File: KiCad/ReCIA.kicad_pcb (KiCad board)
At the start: 2 copper layers, 17.4 x 51.4 mm, 1 part, among them U1 8520_DIP

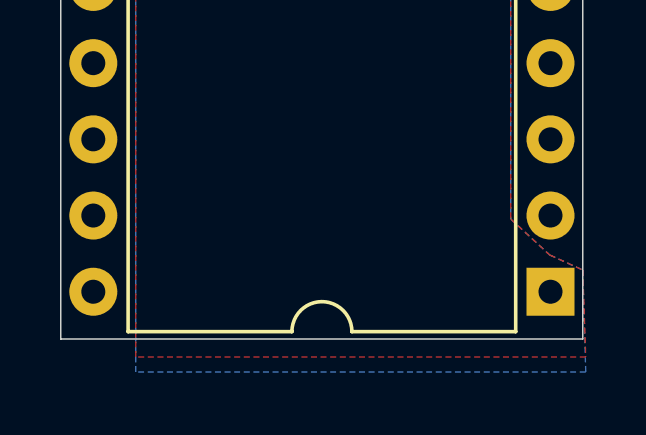
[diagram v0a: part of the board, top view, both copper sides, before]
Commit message: Changed to four layers and fixed clearance and default settings for traces and vias etc
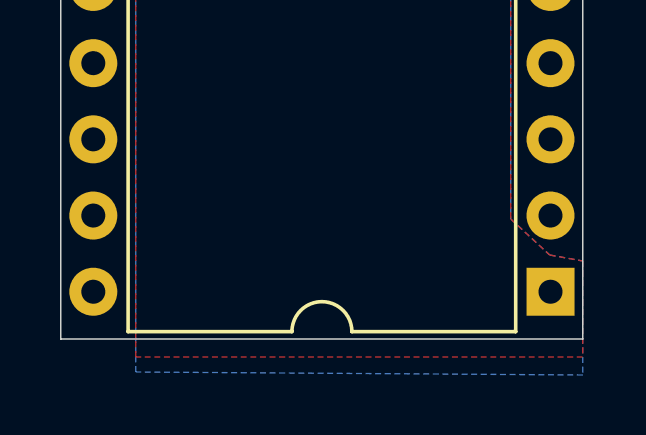
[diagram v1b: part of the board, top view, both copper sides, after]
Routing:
- added copper zone on 3V3, net (none)
- added copper zone on GND, net GND
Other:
- copper layers 2 -> 4
- net class Default: clearance 0.2 -> 0.15; trace_width 0.25 -> 0.15
- rule trace_clearance: 0.2 -> 0.15
- rule trace_min: 0.2 -> 0.15
- rule via_min_drill: 0.3 -> 0.25
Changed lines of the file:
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@@
   (layers
     (0 F.Cu signal)
+    (1 GND power)
+    (2 3V3 power)
     (31 B.Cu signal)
     (32 B.Adhes user)
@@
   )
   (setup
-    (last_trace_width 0.25)
-    (trace_clearance 0.2)
-    (zone_clearance 0.508)
+    (last_trace_width 0.15)
+    (user_trace_width 0.2)
+    (user_trace_width 0.25)
+    (trace_clearance 0.15)
+    (zone_clearance 0.15)
     (zone_45_only no)
-    (trace_min 0.2)
+    (trace_min 0.15)
     (via_size 0.8)
     (via_drill 0.4)
     (via_min_size 0.4)
-    (via_min_drill 0.3)
+    (via_min_drill 0.25)
+    (user_via 0.4 0.25)
     (uvia_size 0.3)
     (uvia_drill 0.1)
@@
   (net 40 GND)
   (net_class Default "This is the default net class."
-    (clearance 0.2)
-    (trace_width 0.25)
+    (clearance 0.15)
+    (trace_width 0.15)
     (via_dia 0.8)
     (via_drill 0.4)
@@
       (effects (font (size 1 1) (thickness 0.15)))
     )
+    (fp_line (start -6.37008 -25.39492) (end 7.35992 -25.39492) (layer F.Fab) (width 0.1))
+    (fp_line (start 7.35992 -25.39492) (end 7.35992 25.40508) (layer F.Fab) (width 0.1))
+    (fp_line (start 7.35992 25.40508) (end -7.37008 25.40508) (layer F.Fab) (width 0.1))
+    (fp_line (start -7.37008 25.40508) (end -7.37008 -24.39492) (layer F.Fab) (width 0.1))
+    (fp_line (start -7.37008 -24.39492) (end -6.37008 -25.39492) (layer F.Fab) (width 0.1))
+    (fp_line (start -1.00508 -25.45492) (end -6.46508 -25.45492) (layer F.SilkS) (width 0.12))
+    (fp_line (start -6.46508 -25.45492) (end -6.46508 25.46508) (layer F.SilkS) (width 0.12))
+    (fp_line (start -6.46508 25.46508) (end 6.45492 25.46508) (layer F.SilkS) (width 0.12))
+    (fp_line (start 6.45492 25.46508) (end 6.45492 -25.45492) (layer F.SilkS) (width 0.12))
+    (fp_line (start 6.45492 -25.45492) (end 0.99492 -25.45492) (layer F.SilkS) (width 0.12))
+    (fp_line (start -8.67508 -25.67492) (end -8.67508 25.67508) (layer F.CrtYd) (width 0.05))
+    (fp_line (start -8.67508 25.67508) (end 8.67492 25.67508) (layer F.CrtYd) (width 0.05))
+    (fp_line (start 8.67492 25.67508) (end 8.67492 -25.67492) (layer F.CrtYd) (width 0.05))
     (fp_line (start 8.67492 -25.67492) (end -8.67508 -25.67492) (layer F.CrtYd) (width 0.05))
-    (fp_line (start 8.67492 25.67508) (end 8.67492 -25.67492) (layer F.CrtYd) (width 0.05))
-    (fp_line (start -8.67508 25.67508) (end 8.67492 25.67508) (layer F.CrtYd) (width 0.05))
-    (fp_line (start -8.67508 -25.67492) (end -8.67508 25.67508) (layer F.CrtYd) (width 0.05))
-    (fp_line (start 6.45492 -25.45492) (end 0.99492 -25.45492) (layer F.SilkS) (width 0.12))
-    (fp_line (start 6.45492 25.46508) (end 6.45492 -25.45492) (layer F.SilkS) (width 0.12))
-    (fp_line (start -6.46508 25.46508) (end 6.45492 25.46508) (layer F.SilkS) (width 0.12))
-    (fp_line (start -6.46508 -25.45492) (end -6.46508 25.46508) (layer F.SilkS) (width 0.12))
-    (fp_line (start -1.00508 -25.45492) (end -6.46508 -25.45492) (layer F.SilkS) (width 0.12))
-    (fp_line (start -7.37008 -24.39492) (end -6.37008 -25.39492) (layer F.Fab) (width 0.1))
-    (fp_line (start -7.37008 25.40508) (end -7.37008 -24.39492) (layer F.Fab) (width 0.1))
-    (fp_line (start 7.35992 25.40508) (end -7.37008 25.40508) (layer F.Fab) (width 0.1))
-    (fp_line (start 7.35992 -25.39492) (end 7.35992 25.40508) (layer F.Fab) (width 0.1))
-    (fp_line (start -6.37008 -25.39492) (end 7.35992 -25.39492) (layer F.Fab) (width 0.1))
     (fp_text user %R (at -0.00508 0.00508) (layer F.Fab) hide
       (effects (font (size 1 1) (thickness 0.15)))
@@
       (net 36 "Net-(U1-Pad22)"))
     (pad 2 thru_hole oval (at -7.62508 -21.58492 180) (size 1.6 1.6) (drill 0.8) (layers *.Cu *.Mask)
-      (net 37 "Net-(U1-Pad2)"))
+      (net 37 "Net-(U1-Pad2)") (clearance 0.5))
     (pad 21 thru_hole oval (at 7.61492 24.13508 180) (size 1.6 1.6) (drill 0.8) (layers *.Cu *.Mask)
       (net 38 "Net-(U1-Pad21)"))
     (pad 1 thru_hole rect (at -7.62508 -24.12492 180) (size 1.6 1.6) (drill 0.8) (layers *.Cu *.Mask)
-      (net 40 GND) (zone_connect 2))
+      (net 40 GND) (zone_connect 2) (thermal_gap 0.5))
   )
   (gr_line (start 123.3 108.7) (end 123.3 57.3) (layer Edge.Cuts) (width 0.05))
@@
   (gr_line (start 123.3 57.3) (end 140.7 57.3) (layer Edge.Cuts) (width 0.05))
   (zone (net 40) (net_name GND) (layer F.Cu) (hatch edge 0.508)
-    (connect_pads (clearance 0.508))
-    (min_thickness 0.254)
-    (fill yes (arc_segments 32) (thermal_gap 0.508) (thermal_bridge_width 0.508))
+    (connect_pads (clearance 0.15))
+    (min_thickness 0.15)
+    (fill yes (arc_segments 32) (thermal_gap 0.15) (thermal_bridge_width 0.3))
     (polygon
       (pts
-        (xy 138.3 104.7) (xy 139.6 105.9) (xy 140.7 106.4) (xy 140.8 109.3) (xy 125.8 109.3)
+        (xy 138.3 104.7) (xy 139.6 105.9) (xy 140.7 106.1) (xy 140.7 109.3) (xy 125.8 109.3)
         (xy 125.8 56.8) (xy 138.3 56.8)
       )
@@
   )
   (zone (net 40) (net_name GND) (layer B.Cu) (hatch edge 0.508)
-    (connect_pads (clearance 0.508))
-    (min_thickness 0.254)
-    (fill yes (arc_segments 32) (thermal_gap 0.508) (thermal_bridge_width 0.508))
+    (connect_pads (clearance 0.15))
+    (min_thickness 0.15)
+    (fill yes (arc_segments 32) (thermal_gap 0.15) (thermal_bridge_width 0.3))
     (polygon
       (pts
-        (xy 138.3 104.7) (xy 139.6 105.9) (xy 140.7 106.4) (xy 140.8 109.8) (xy 125.8 109.8)
+        (xy 138.3 104.7) (xy 139.6 105.9) (xy 140.7 106.1) (xy 140.7 109.9) (xy 125.8 109.8)
         (xy 125.8 56.3) (xy 138.3 56.3)
       )
     )
+  )
+  (zone (net 40) (net_name GND) (layer GND) (hatch edge 0.508)
+    (connect_pads (clearance 0.15))
+    (min_thickness 0.15)
+    (fill yes (arc_segments 32) (thermal_gap 0.15) (thermal_bridge_width 0.3))
+    (polygon
+      (pts
+        (xy 138.3 104.7) (xy 139.6 105.9) (xy 140.7 106.1) (xy 140.7 110.4) (xy 125.8 110.3)
+        (xy 125.8 55.8) (xy 138.3 55.8)
+      )
+    )
+  )
+  (zone (net 0) (net_name "") (layer 3V3) (hatch edge 0.508)
+    (connect_pads (clearance 0.15))
+    (min_thickness 0.15)
+    (fill yes (arc_segments 32) (thermal_gap 0.15) (thermal_bridge_width 0.3))
+    (polygon
+      (pts
+        (xy 138.3 110.9) (xy 125.8 110.9) (xy 125.8 55.3) (xy 138.3 55.3)
+      )
+    )

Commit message: Add nets
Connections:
- net Net-(U1-Pad10) renamed PB0
- net Net-(U1-Pad11) renamed PB1
- net Net-(U1-Pad12) renamed PB2
- net Net-(U1-Pad13) renamed PB3
- net Net-(U1-Pad14) renamed PB4
- net Net-(U1-Pad15) renamed PB5
- net Net-(U1-Pad16) renamed PB6
- net Net-(U1-Pad17) renamed PB7
- net Net-(U1-Pad18) renamed PC
- net Net-(U1-Pad19) renamed TOD
- net Net-(U1-Pad2) renamed PA0
- net Net-(U1-Pad21) renamed IRQ
- net Net-(U1-Pad22) renamed RW
- net Net-(U1-Pad23) renamed CS
- net Net-(U1-Pad24) renamed FLAG
- net Net-(U1-Pad25) renamed E-CLK
- net Net-(U1-Pad26) renamed D7
- net Net-(U1-Pad27) renamed D6
- net Net-(U1-Pad28) renamed D5
- net Net-(U1-Pad29) renamed D4
- net Net-(U1-Pad3) renamed PA1
- net Net-(U1-Pad30) renamed D3
- net Net-(U1-Pad31) renamed D2
- net Net-(U1-Pad32) renamed D1
- net Net-(U1-Pad33) renamed D0
- net Net-(U1-Pad34) renamed RESET
- net Net-(U1-Pad35) renamed A3
- net Net-(U1-Pad36) renamed A2
- net Net-(U1-Pad37) renamed A1
- net Net-(U1-Pad38) renamed A0
- net Net-(U1-Pad39) renamed SP
- net Net-(U1-Pad4) renamed PA2
- net Net-(U1-Pad40) renamed CNT
- net Net-(U1-Pad5) renamed PA3
- net Net-(U1-Pad6) renamed PA4
- net Net-(U1-Pad7) renamed PA5
- net Net-(U1-Pad8) renamed PA6
- net Net-(U1-Pad9) renamed PA7

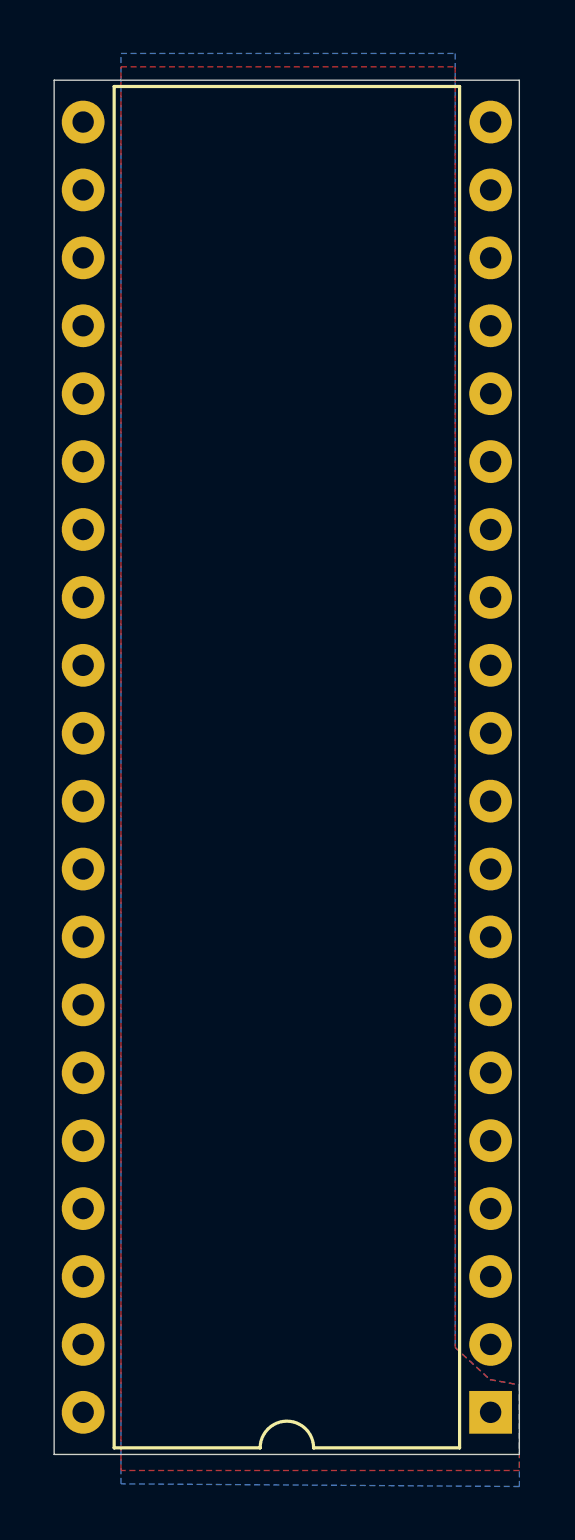
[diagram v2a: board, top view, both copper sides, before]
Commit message: Added a 3.3V LDO Voltage Regulator
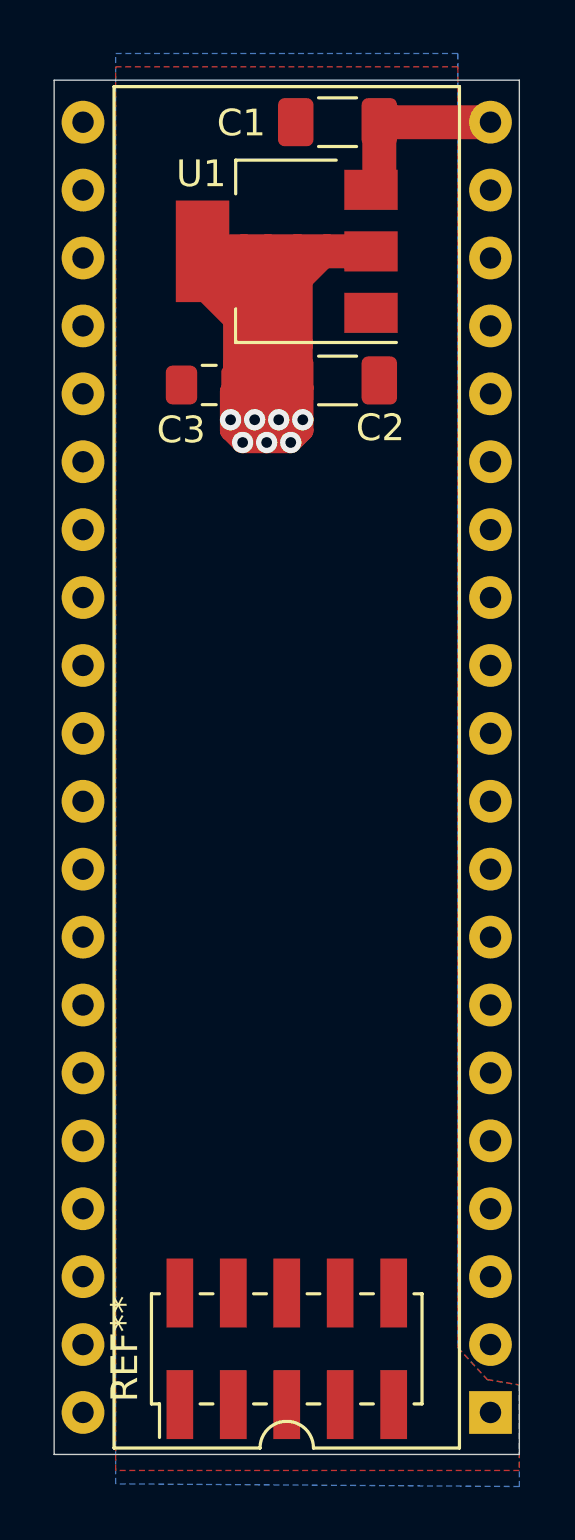
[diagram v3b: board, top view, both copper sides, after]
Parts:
- added C1: 10uF, Capacitor_SMD:C_1206_3216Metric_Pad1.33x1.80mm_HandSolder, F.Cu at (133.9, 58.9)
- added C2: 10uF, Capacitor_SMD:C_1206_3216Metric_Pad1.33x1.80mm_HandSolder, F.Cu at (133.9, 68.5)
- added C3: 0.1uF, Capacitor_SMD:C_0805_2012Metric_Pad1.18x1.45mm_HandSolder, F.Cu at (129.1, 68.7)
- added REF**: PinHeader_2x05_P2.00mm_Vertical_SMD, Connector_PinHeader_2.00mm:PinHeader_2x05_P2.00mm_Vertical_SMD, F.Cu at (132.0, 104.8)
- added U5: 8520_DIP, Package_DIP:DIP-40_W15.24mm, F.Cu at (132.0, 83.0)
- U1: value 8520_DIP -> AMS1117-3.3; footprint Package_DIP:DIP-40_W15.24mm -> Package_TO_SOT_SMD:SOT-223-3_TabPin2
- moved U1 19.3 mm to (132.0, 63.7)
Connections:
- U1 pad 2: PA0 -> 3V3
- U1 pad 3: PA1 -> VCC
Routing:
- net 3V3: track 0.00 -> 63.2 mm, vias 0 -> 7
- net VCC: track 0.00 -> 6.82 mm
- added copper zone on 3V3, net 3V3
- removed copper zone on 3V3, net (none)

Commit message: Add 10 Max FPGA
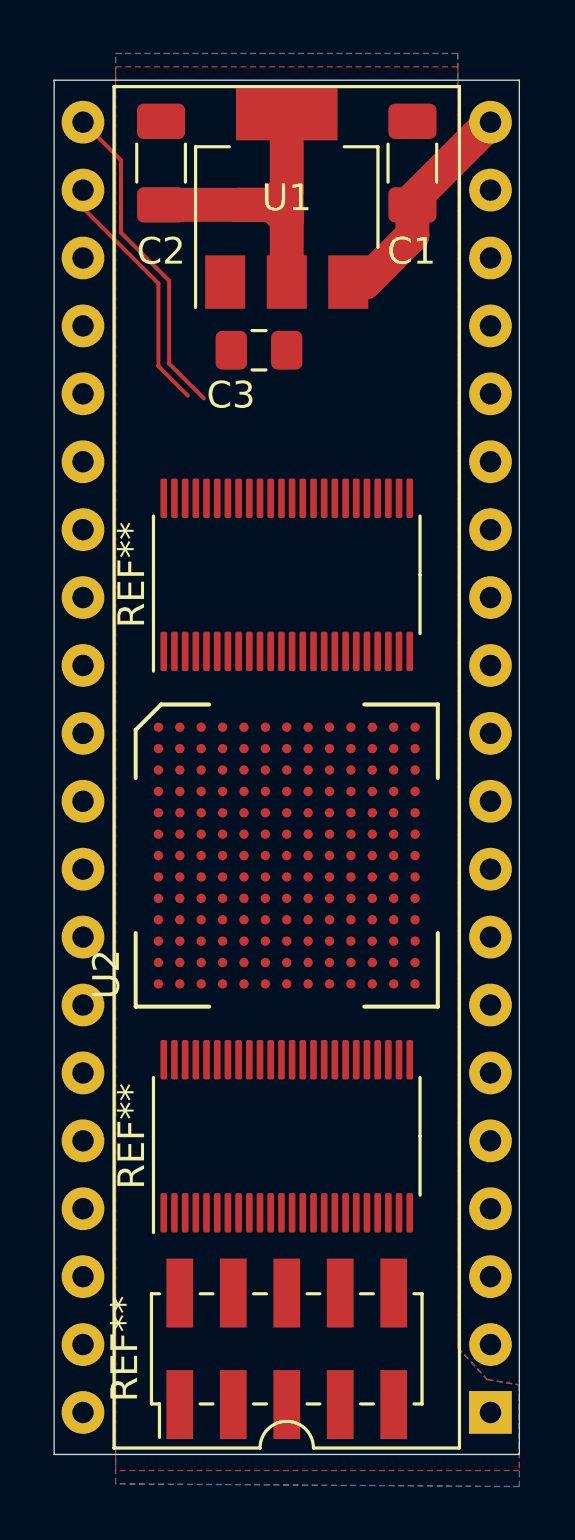
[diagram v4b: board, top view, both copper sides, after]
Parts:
- added REF**: TSSOP-48_4.4x9.7mm_P0.4mm, Package_SO:TSSOP-48_4.4x9.7mm_P0.4mm, F.Cu at (132.0, 96.8)
- added REF**: TSSOP-48_4.4x9.7mm_P0.4mm, Package_SO:TSSOP-48_4.4x9.7mm_P0.4mm, F.Cu at (132.0, 75.8)
- added U2: 10M02SCU169, ReCIA:BGA-169_11.0x11.0mm_Layout13x13_P0.8mm_Ball0.5mm_Pad0.35mm_NSMD, F.Cu at (132.0, 86.3)
- moved C2 10.5 mm to (127.3, 60.4), turned to 90 degrees
- moved C1 3.19 mm to (136.7, 60.4), turned to 90 degrees
- moved C3 2.27 mm to (131.0, 67.4)
- moved U1 2.00 mm to (132.0, 61.7), turned to 90 degrees
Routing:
- net 3V3: track 63.2 -> 15.2 mm, vias 7 -> 0
- net IRQ: track 0.00 -> 12.2 mm
- net RW: track 0.00 -> 9.31 mm
- net VCC: track 6.82 -> 8.56 mm
